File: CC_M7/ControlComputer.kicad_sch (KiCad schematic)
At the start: 38 parts, among them U1 STM32H743VITx, Y1 32MHz

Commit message: Scehmatic completed.
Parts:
- removed U1: STM32H743VITx, Package_QFP:LQFP-100_14x14mm_P0.5mm, symbol MCU_ST_STM32H7:STM32H743VITx
- added U1: STM32H743VGTx, Package_QFP:LQFP-100_14x14mm_P0.5mm, symbol MCU_ST_STM32H7:STM32H743VGTx
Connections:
- net +3.3V: now also U1.100 (VDD), U1.11 (VDD), U1.27 (VDD), U1.50 (VDD), U1.6 (VBAT), U1.75 (VDD)
- net BOOT0: now also U1.94 (BOOT0)
- net CAN2_RX: now also U1.51 (PB12)
- net CAN2_TX: now also U1.52 (PB13)
- net GND: now also U1.10 (VSS), U1.19 (VSSA), U1.26 (VSS), U1.49 (VSS), U1.74 (VSS), U1.99 (VSS)
- net HSE_IN: now also U1.12 (PH0)
- net HSE_OUT: now also U1.13 (PH1)
- net I2C1_IRQ1: now also U1.43 (PE13)
- net I2C1_IRQ2: now also U1.44 (PE14)
- net I2C1_SCL: now also U1.92 (PB6)
- net I2C1_SDA: now also U1.93 (PB7)
- net I2C2_SCL: now also U1.46 (PB10)
- net I2C2_SDA: now also U1.47 (PB11)
- net LED0: now also U1.40 (PE10)
- net LED1: now also U1.41 (PE11)
- net NRST: now also U1.14 (NRST)
- net PA0: now also U1.22 (PA0)
- net PA1: now also U1.23 (PA1)
- net PA4: now also U1.28 (PA4)
- net PC13: now also U1.7 (PC13)
- net PC14: now also U1.8 (PC14)
- net PC15: now also U1.9 (PC15)
- net PE2: now also U1.1 (PE2)
- net PE3: now also U1.2 (PE3)
- net PE4: now also U1.3 (PE4)
- net PE5: now also U1.4 (PE5)
- net PE6: now also U1.5 (PE6)
- net SPI1_CS1: now also U1.32 (PC4)
- net SPI1_CS2: now also U1.33 (PC5)
- net SPI1_CS3: now also U1.34 (PB0)
- net SPI1_MISO: now also U1.30 (PA6)
- net SPI1_MOSI: now also U1.31 (PA7)
- net SPI1_SCK: now also U1.29 (PA5)
- net SPI3_CS: now also U1.81 (PD0)
- net SPI3_IRQ: now also U1.82 (PD1)
- net SPI3_MISO: now also U1.79 (PC11)
- net SPI3_MOSI: now also U1.80 (PC12)
- net SPI3_SCK: now also U1.78 (PC10)
- net SWCLK: now also U1.76 (PA14)
- net SWDIO: now also U1.72 (PA13)
- net SWO: now also U1.89 (PB3)
- net TIM3_CH1: now also U1.63 (PC6)
- net TIM3_CH2: now also U1.64 (PC7)
- net TIM3_CH3: now also U1.65 (PC8)
- net TIM3_CH4: now also U1.66 (PC9)
- net TIM4_CH3: now also U1.61 (PD14)
- net TIM4_CH4: now also U1.62 (PD15)
- net UART1_RX: now also U1.69 (PA10)
- net UART1_TX: now also U1.68 (PA9)
- net UART2_RX: now also U1.25 (PA3)
- net UART2_TX: now also U1.24 (PA2)
- net UART3_RX: now also U1.56 (PD9)
- net UART3_TX: now also U1.55 (PD8)
- net UART4_RX: now also U1.95 (PB8)
- net UART4_TX: now also U1.96 (PB9)
- net USB_DM: now also U1.70 (PA11)
- net USB_DP: now also U1.71 (PA12)
- net VDDA_CC: now also U1.21 (VDDA)
- net VREF_CC: now also U1.20 (VREF+)
- net at C17.1: now also U1.48 (VCAP)
- net at C18.1: now also U1.73 (VCAP)
- no-connect marks 28 -> 29
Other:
- note removed: "STM32H743VGT6"
- moved on the sheet: C1, C10, C12, C13, C14, C15, C17, C18, C2, C20, C21, C4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

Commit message: last control
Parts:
- added JP9: SWDIO, jmpertest:jmpertest, symbol Jumper:Jumper_2_Bridged
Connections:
- net J2_38 is gone; now on net J2_36: JP3.2 (B)
- net +3.3V: now also JP9.1 (A)
- net J2_36: no longer JP2.2 (B)
- net SWDIO: now also JP1.1 (A); no longer JP3.1 (A)
- net SWO: now also JP3.1 (A); no longer JP1.1 (A)
- net PE5: no longer names the net of U1.4 (PE5)
- net PE6: no longer names the net of U1.5 (PE6)
- new net J2_31: JP9.2 (B)
- new net J2_34: JP2.2 (B)
- no-connect marks 29 -> 31
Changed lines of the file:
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@@
 	)
 	(no_connect
+		(at 45.72 147.32)
+	)
+	(no_connect
 		(at 45.72 190.5)
 	)
 	(no_connect
+		(at 45.72 149.86)
+	)
+	(no_connect
 		(at 45.72 210.82)
 	)
@@
 	(wire
 		(pts
+			(xy 152.4 200.66) (xy 160.02 200.66)
+		)
+		(stroke
+			(width 0)
+			(type default)
+		)
+	)
+	(wire
+		(pts
 			(xy 96.52 27.94) (xy 96.52 30.48)
 		)
@@
 		)
 	)
+	(global_label "J2_40"
+		(shape input)
+		(at 170.18 220.98 0)
+		(fields_autoplaced yes)
+		(effects
+			(font
+				(size 1.27 1.27)
+			)
+			(justify left)
+		)
+		(property "Intersheetrefs" "${INTERSHEET_REFS}"
+			(at 178.7289 220.98 0)
+			(effects
+				(font
+					(size 1.27 1.27)
+				)
+				(justify left)
+				(hide yes)
+			)
+		)
+	)
 	(global_label "UART1_TX"
 		(shape input)
@@
 		)
 	)
+	(global_label "J2_36"
+		(shape input)
+		(at 170.18 215.9 0)
+		(fields_autoplaced yes)
+		(effects
+			(font
+				(size 1.27 1.27)
+			)
+			(justify left)
+		)
+		(property "Intersheetrefs" "${INTERSHEET_REFS}"
+			(at 178.7289 215.9 0)
+			(effects
+				(font
+					(size 1.27 1.27)
+				)
+				(justify left)
+				(hide yes)
+			)
+		)
+	)
 	(global_label "LED0"
 		(shape input)
@@
 	(global_label "SWO"
 		(shape input)
-		(at 160.02 205.74 180)
+		(at 160.02 215.9 180)
 		(fields_autoplaced yes)
 		(effects
@@
 		)
 		(property "Intersheetrefs" "${INTERSHEET_REFS}"
-			(at 153.0434 205.74 0)
+			(at 153.0434 215.9 0)
 			(effects
 				(font
@@
 		)
 	)
+	(global_label "J2_32"
+		(shape input)
+		(at 170.18 205.74 0)
+		(fields_autoplaced yes)
+		(effects
+			(font
+				(size 1.27 1.27)
+			)
+			(justify left)
+		)
+		(property "Intersheetrefs" "${INTERSHEET_REFS}"
+			(at 178.7289 205.74 0)
+			(effects
+				(font
+					(size 1.27 1.27)
+				)
+				(justify left)
+				(hide yes)
+			)
+		)
+	)
 	(global_label "UART4_RX"
 		(shape input)
@@
 		)
 	)
+	(global_label "J2_31"
+		(shape input)
+		(at 170.18 200.66 0)
+		(fields_autoplaced yes)
+		(effects
+			(font
+				(size 1.27 1.27)
+			)
+			(justify left)
+		)
+		(property "Intersheetrefs" "${INTERSHEET_REFS}"
+			(at 178.7289 200.66 0)
+			(effects
+				(font
+					(size 1.27 1.27)
+				)
+				(justify left)
+				(hide yes)
+			)
+		)
+	)
 	(global_label "SPI1_CS1"
 		(shape input)
@@
 		)
 	)
+	(global_label "J2_34"
+		(shape input)
+		(at 170.18 210.82 0)
+		(fields_autoplaced yes)
+		(effects
+			(font
+				(size 1.27 1.27)
+			)
+			(justify left)
+		)
+		(property "Intersheetrefs" "${INTERSHEET_REFS}"
+			(at 178.7289 210.82 0)
+			(effects
+				(font
+					(size 1.27 1.27)
+				)
+				(justify left)
+				(hide yes)
+			)
+		)
+	)
 	(global_label "SWDIO"
 		(shape input)
-		(at 160.02 215.9 180)
+		(at 160.02 205.74 180)
 		(fields_autoplaced yes)
 		(effects
@@
 		)
 		(property "Intersheetrefs" "${INTERSHEET_REFS}"
-			(at 151.1686 215.9 0)
+			(at 151.1686 205.74 0)
 			(effects
 				(font
@@
 		)
 	)
-	(global_label "PE6"
-		(shape input)
-		(at 45.72 149.86 180)
-		(fields_autoplaced yes)
-		(effects
-			(font
-				(size 1.27 1.27)
-			)
-			(justify right)
-		)
-		(property "Intersheetrefs" "${INTERSHEET_REFS}"
-			(at 39.1063 149.86 0)
-			(effects
-				(font
-					(size 1.27 1.27)
-				)
-				(justify right)
-				(hide yes)
-			)
-		)
-	)
-	(global_label "J2_40"
-		(shape input)
-		(at 170.18 220.98 0)
-		(fields_autoplaced yes)
-		(effects
-			(font
-				(size 1.27 1.27)
-			)
-			(justify left)
-		)
-		(property "Intersheetrefs" "${INTERSHEET_REFS}"
-			(at 178.7289 220.98 0)
-			(effects
-				(font
-					(size 1.27 1.27)
-				)
-				(justify left)
-				(hide yes)
-			)
-		)
-	)
 	(global_label "SPI3_SCK"
 		(shape input)
@@
 		)
 	)
-	(global_label "PE5"
-		(shape input)
-		(at 45.72 147.32 180)
-		(fields_autoplaced yes)
-		(effects
-			(font
-				(size 1.27 1.27)
-			)
-			(justify right)
-		)
-		(property "Intersheetrefs" "${INTERSHEET_REFS}"
-			(at 39.1063 147.32 0)
-			(effects
-				(font
-					(size 1.27 1.27)
-				)
-				(justify right)
-				(hide yes)
-			)
-		)
-	)
 	(global_label "HSE_OUT"
 		(shape input)
@@
 		)
 	)
-	(global_label "J2_32"
-		(shape input)
-		(at 170.18 205.74 0)
-		(fields_autoplaced yes)
-		(effects
-			(font
-				(size 1.27 1.27)
-			)
-			(justify left)
-		)
-		(property "Intersheetrefs" "${INTERSHEET_REFS}"
-			(at 178.7289 205.74 0)
-			(effects
-				(font
-					(size 1.27 1.27)
-				)
-				(justify left)
-				(hide yes)
-			)
-		)
-	)
 	(global_label "NRST"
 		(shape input)
@@
 		)
 	)
-	(global_label "J2_38"
-		(shape input)
-		(at 170.18 215.9 0)
-		(fields_autoplaced yes)
-		(effects
-			(font
-				(size 1.27 1.27)
-			)
-			(justify left)
-		)
-		(property "Intersheetrefs" "${INTERSHEET_REFS}"
-			(at 178.7289 215.9 0)
-			(effects
-				(font
-					(size 1.27 1.27)
-				)
-				(justify left)
-				(hide yes)
-			)
-		)
-	)
-	(global_label "J2_36"
-		(shape input)
-		(at 170.18 210.82 0)
-		(fields_autoplaced yes)
-		(effects
-			(font
-				(size 1.27 1.27)
-			)
-			(justify left)
-		)
-		(property "Intersheetrefs" "${INTERSHEET_REFS}"
-			(at 178.7289 210.82 0)
-			(effects
-				(font
-					(size 1.27 1.27)
-				)
-				(justify left)
-				(hide yes)
-			)
-		)
-	)
 	(global_label "PA1"
 		(shape input)
@@
 	)
 	(symbol
+		(lib_id "Jumper:Jumper_2_Bridged")
+		(at 165.1 200.66 0)
+		(unit 1)
+		(exclude_from_sim yes)
+		(in_bom yes)
+		(on_board yes)
+		(dnp no)
+		(property "Reference" "JP9"
+			(at 165.1 198.12 0)
+			(effects
+				(font
+					(size 1.27 1.27)
+				)
+			)
+		)
+		(property "Value" "SWDIO"
+			(at 165.1 198.12 0)
+			(effects
+				(font
+					(size 1.27 1.27)
+				)
+				(hide yes)
+			)
+		)
+		(property "Footprint" "jmpertest:jmpertest"
+			(at 165.1 200.66 0)
+			(effects
+				(font
+					(size 1.27 1.27)
+				)
+				(hide yes)
+			)
+		)
+		(property "Datasheet" "~"
+			(at 165.1 200.66 0)
+			(effects
+				(font
+					(size 1.27 1.27)
+				)
+				(hide yes)
+			)
+		)
+		(property "Description" "Jumper, 2-pole, closed/bridged"
+			(at 165.1 200.66 0)
+			(effects
+				(font
+					(size 1.27 1.27)
+				)
+				(hide yes)
+			)
+		)
+		(pin "2"
+		)
+		(pin "1"
+		)
+		(instances
+			(project "CC_M7"
+				(path "/20c3bbae-00c6-470e-8b69-dc0f665257a3/07f6f905-59c0-438f-a556-b28e89ace803"
+					(reference "JP9")
+					(unit 1)
+				)
+			)
+		)
+	)
+	(symbol
 		(lib_id "Device:R_Small")
 		(at 165.1 175.26 270)
@@
 					(unit 1)
 				)
+			)
+		)
+	)
+	(symbol
+		(lib_id "power:+3.3V")
+		(at 152.4 200.66 90)
+		(unit 1)
+		(exclude_from_sim no)
+		(in_bom yes)
+		(on_board yes)
+		(dnp no)
+		(fields_autoplaced yes)
+		(property "Reference" "#PWR039"
+			(at 156.21 200.66 0)
+			(effects
+				(font
+					(size 1.27 1.27)
+				)
+				(hide yes)
+			)
+		)
+		(property "Value" "+3.3V"
+			(at 148.59 200.6599 90)
+			(effects
+				(font
+					(size 1.27 1.27)
+				)
+				(justify left)
+			)
+		)
+		(property "Footprint" ""
+			(at 152.4 200.66 0)
+			(effects
+				(font
+					(size 1.27 1.27)
+				)
+				(hide yes)
+			)
+		)
+		(property "Datasheet" ""
+			(at 152.4 200.66 0)
+			(effects
+				(font
+					(size 1.27 1.27)
+				)
+				(hide yes)
+			)
+		)
+		(property "Description" "Power symbol creates a global label with name \"+3.3V\""
+			(at 152.4 200.66 0)
+			(effects
+				(font
+					(size 1.27 1.27)
+				)
+				(hide yes)
+			)
+		)
+		(pin "1"
+		)
+		(instances
+			(project "CC_M7"
+				(path "/20c3bbae-00c6-470e-8b69-dc0f665257a3/07f6f905-59c0-438f-a556-b28e89ace803"
+					(reference "#PWR039")
+					(unit 1)
+				)

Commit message: ready for routing
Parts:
- removed JP9: SWDIO, jmpertest:jmpertest, symbol Jumper:Jumper_2_Bridged
- added JP5: SWDIO, Jumper:SolderJumper-2_P1.3mm_Open_TrianglePad1.0x1.5mm, symbol Jumper:Jumper_2_Bridged
- C1: footprint Capacitor_SMD:C_0603_1608Metric -> Capacitor_SMD:C_0402_1005Metric
- JP1, JP2, JP3, JP4: footprint jmpertest:jmpertest -> Jumper:SolderJumper-2_P1.3mm_Open_TrianglePad1.0x1.5mm
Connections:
- net +3.3V: now also JP1.1 (A)
- net J2_31: now also JP1.2 (B)
- net J2_32: now also JP2.2 (B); no longer JP1.2 (B)
- net J2_34: now also JP3.2 (B); no longer JP2.2 (B)
- net J2_36: now also JP4.2 (B); no longer JP3.2 (B)
- net J2_40: now also JP5.2 (B); no longer JP4.2 (B)
- net NRST: now also JP5.1 (A); no longer JP4.1 (A)
- net SWCLK: now also JP3.1 (A); no longer JP2.1 (A)
- net SWDIO: now also JP2.1 (A); no longer JP1.1 (A)
- net SWO: now also JP4.1 (A); no longer JP3.1 (A)
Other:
- moved on the sheet: JP1, JP2, JP3, JP4
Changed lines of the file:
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@@
 	(text "OSC STM32"
 		(exclude_from_sim no)
-		(at 182.88 121.92 0)
+		(at 180.975 121.92 0)
 		(effects
 			(font
@@
 	(text "I2C PULL_UP"
 		(exclude_from_sim no)
-		(at 180.34 157.48 0)
+		(at 179.07 157.48 0)
 		(effects
 			(font
@@
 	(text "VDDA FILTER"
 		(exclude_from_sim no)
-		(at 116.84 83.82 0)
+		(at 115.57 83.82 0)
 		(effects
 			(font
@@
 	)
 	(symbol
-		(lib_id "Jumper:Jumper_2_Bridged")
-		(at 165.1 200.66 0)
-		(unit 1)
-		(exclude_from_sim yes)
-		(in_bom yes)
-		(on_board yes)
-		(dnp no)
-		(property "Reference" "JP9"
-			(at 165.1 198.12 0)
-			(effects
-				(font
-					(size 1.27 1.27)
-				)
-			)
-		)
-		(property "Value" "SWDIO"
-			(at 165.1 198.12 0)
-			(effects
-				(font
-					(size 1.27 1.27)
-				)
-				(hide yes)
-			)
-		)
-		(property "Footprint" "jmpertest:jmpertest"
-			(at 165.1 200.66 0)
-			(effects
-				(font
-					(size 1.27 1.27)
-				)
-				(hide yes)
-			)
-		)
-		(property "Datasheet" "~"
-			(at 165.1 200.66 0)
-			(effects
-				(font
-					(size 1.27 1.27)
-				)
-				(hide yes)
-			)
-		)
-		(property "Description" "Jumper, 2-pole, closed/bridged"
-			(at 165.1 200.66 0)
-			(effects
-				(font
-					(size 1.27 1.27)
-				)
-				(hide yes)
-			)
-		)
-		(pin "2"
-		)
-		(pin "1"
-		)
-		(instances
-			(project "CC_M7"
-				(path "/20c3bbae-00c6-470e-8b69-dc0f665257a3/07f6f905-59c0-438f-a556-b28e89ace803"
-					(reference "JP9")
-					(unit 1)
-				)
-			)
-		)
-	)
-	(symbol
 		(lib_id "Device:R_Small")
 		(at 165.1 175.26 270)
@@
 	(symbol
 		(lib_id "Jumper:Jumper_2_Bridged")
-		(at 165.1 220.98 0)
+		(at 165.1 215.9 0)
 		(unit 1)
 		(exclude_from_sim yes)
@@
 		(dnp no)
 		(property "Reference" "JP4"
-			(at 165.1 218.44 0)
+			(at 165.1 213.36 0)
 			(effects
 				(font
@@
 		)
 		(property "Value" "SWDIO"
-			(at 165.1 218.44 0)
+			(at 165.1 213.36 0)
 			(effects
 				(font
@@
 			)
 		)
-		(property "Footprint" "jmpertest:jmpertest"
-			(at 165.1 220.98 0)
+		(property "Footprint" "Jumper:SolderJumper-2_P1.3mm_Open_TrianglePad1.0x1.5mm"
+			(at 165.1 215.9 0)
 			(effects
 				(font
@@
 		)
 		(property "Datasheet" "~"
-			(at 165.1 220.98 0)
+			(at 165.1 215.9 0)
 			(effects
 				(font
@@
 		)
 		(property "Description" "Jumper, 2-pole, closed/bridged"
-			(at 165.1 220.98 0)
+			(at 165.1 215.9 0)
 			(effects
 				(font
@@
 	)
 	(symbol
+		(lib_id "Jumper:Jumper_2_Bridged")
+		(at 165.1 220.98 0)
+		(unit 1)
+		(exclude_from_sim yes)
+		(in_bom yes)
+		(on_board yes)
+		(dnp no)
+		(property "Reference" "JP5"
+			(at 165.1 218.44 0)
+			(effects
+				(font
+					(size 1.27 1.27)
+				)
+			)
+		)
+		(property "Value" "SWDIO"
+			(at 165.1 218.44 0)
+			(effects
+				(font
+					(size 1.27 1.27)
+				)
+				(hide yes)
+			)
+		)
+		(property "Footprint" "Jumper:SolderJumper-2_P1.3mm_Open_TrianglePad1.0x1.5mm"
+			(at 165.1 220.98 0)
+			(effects
+				(font
+					(size 1.27 1.27)
+				)
+				(hide yes)
+			)
+		)
+		(property "Datasheet" "~"
+			(at 165.1 220.98 0)
+			(effects
+				(font
+					(size 1.27 1.27)
+				)
+				(hide yes)
+			)
+		)
+		(property "Description" "Jumper, 2-pole, closed/bridged"
+			(at 165.1 220.98 0)
+			(effects
+				(font
+					(size 1.27 1.27)
+				)
+				(hide yes)
+			)
+		)
+		(pin "2"
+		)
+		(pin "1"
+		)
+		(instances
+			(project "CC_M7"
+				(path "/20c3bbae-00c6-470e-8b69-dc0f665257a3/07f6f905-59c0-438f-a556-b28e89ace803"
+					(reference "JP5")
+					(unit 1)
+				)
+			)
+		)
+	)
+	(symbol
 		(lib_id "Device:R_Small")
 		(at 162.56 142.24 180)
@@
 	(symbol
 		(lib_id "Jumper:Jumper_2_Bridged")
-		(at 165.1 210.82 0)
+		(at 165.1 205.74 0)
 		(unit 1)
 		(exclude_from_sim yes)
@@
 		(dnp no)
 		(property "Reference" "JP2"
-			(at 165.1 208.28 0)
+			(at 165.1 203.2 0)
 			(effects
 				(font
@@
 		)
 		(property "Value" "SWDIO"
-			(at 165.1 208.28 0)
+			(at 165.1 203.2 0)
 			(effects
 				(font
@@
 			)
 		)
-		(property "Footprint" "jmpertest:jmpertest"
-			(at 165.1 210.82 0)
+		(property "Footprint" "Jumper:SolderJumper-2_P1.3mm_Open_TrianglePad1.0x1.5mm"
+			(at 165.1 205.74 0)
 			(effects
 				(font
@@
 		)
 		(property "Datasheet" "~"
-			(at 165.1 210.82 0)
+			(at 165.1 205.74 0)
 			(effects
 				(font
@@
 		)
 		(property "Description" "Jumper, 2-pole, closed/bridged"
-			(at 165.1 210.82 0)
+			(at 165.1 205.74 0)
 			(effects
 				(font
@@
 	(symbol
 		(lib_id "Jumper:Jumper_2_Bridged")
-		(at 165.1 215.9 0)
+		(at 165.1 210.82 0)
 		(unit 1)
 		(exclude_from_sim yes)
@@
 		(dnp no)
 		(property "Reference" "JP3"
-			(at 165.1 213.36 0)
+			(at 165.1 208.28 0)
 			(effects
 				(font
@@
 		)
 		(property "Value" "SWDIO"
-			(at 165.1 213.36 0)
+			(at 165.1 208.28 0)
 			(effects
 				(font
@@
 			)
 		)
-		(property "Footprint" "jmpertest:jmpertest"
-			(at 165.1 215.9 0)
+		(property "Footprint" "Jumper:SolderJumper-2_P1.3mm_Open_TrianglePad1.0x1.5mm"
+			(at 165.1 210.82 0)
 			(effects
 				(font
@@
 		)
 		(property "Datasheet" "~"
-			(at 165.1 215.9 0)
+			(at 165.1 210.82 0)
 			(effects
 				(font
@@
 		)
 		(property "Description" "Jumper, 2-pole, closed/bridged"
-			(at 165.1 215.9 0)
+			(at 165.1 210.82 0)
 			(effects
 				(font
@@
 	(symbol
 		(lib_id "Jumper:Jumper_2_Bridged")
-		(at 165.1 205.74 0)
+		(at 165.1 200.66 0)
 		(unit 1)
 		(exclude_from_sim yes)
@@
 		(dnp no)
 		(property "Reference" "JP1"
-			(at 165.1 203.2 0)
+			(at 165.1 198.12 0)
 			(effects
 				(font
@@
 		)
 		(property "Value" "SWDIO"
-			(at 165.1 203.2 0)
+			(at 165.1 198.12 0)
 			(effects
 				(font
@@
 			)
 		)
-		(property "Footprint" "jmpertest:jmpertest"
-			(at 165.1 205.74 0)
+		(property "Footprint" "Jumper:SolderJumper-2_P1.3mm_Open_TrianglePad1.0x1.5mm"
+			(at 165.1 200.66 0)
 			(effects
 				(font
@@
 		)
 		(property "Datasheet" "~"
-			(at 165.1 205.74 0)
+			(at 165.1 200.66 0)
 			(effects
 				(font
@@
 		)
 		(property "Description" "Jumper, 2-pole, closed/bridged"
-			(at 165.1 205.74 0)
+			(at 165.1 200.66 0)
 			(effects
 				(font
@@
 			)
 		)
-		(property "Footprint" "Capacitor_SMD:C_0603_1608Metric"
+		(property "Footprint" "Capacitor_SMD:C_0402_1005Metric"
 			(at 40.64 33.02 0)
 			(effects

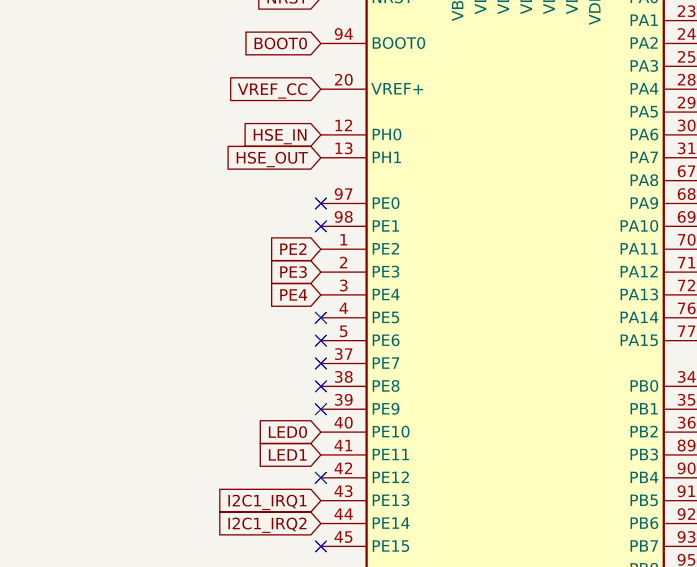
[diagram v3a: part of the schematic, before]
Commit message: ready to routing
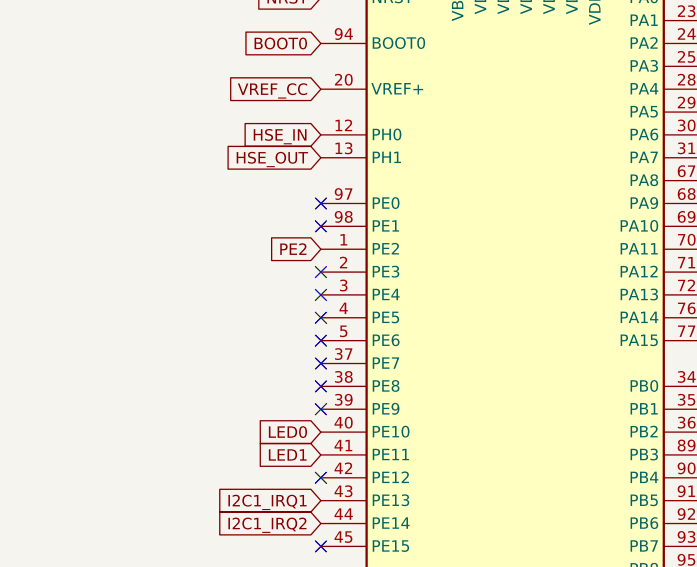
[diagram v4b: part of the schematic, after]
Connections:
- net PE3: no longer names the net of U1.2 (PE3)
- net PE4: no longer names the net of U1.3 (PE4)
- no-connect marks 31 -> 33

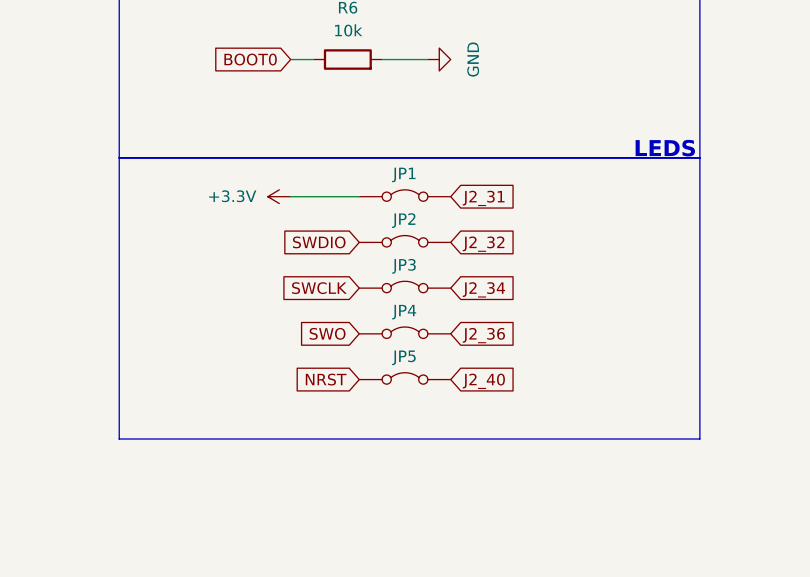
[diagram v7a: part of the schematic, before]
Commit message: Debugging routes added. / Debug footprint updated.
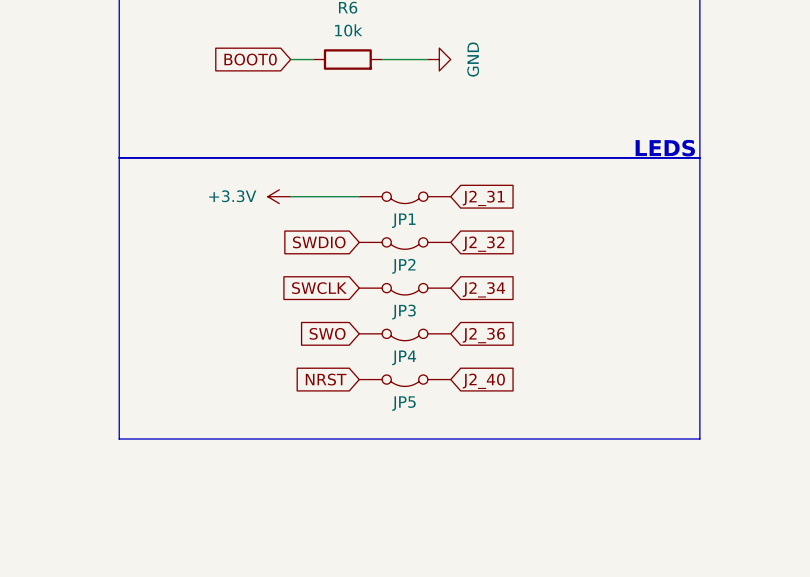
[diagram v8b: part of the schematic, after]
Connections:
- net +3.3V: now also JP1.2 (B); no longer JP1.1 (A)
- net J2_31: now also JP1.1 (A); no longer JP1.2 (B)
- net J2_32: now also JP2.1 (A); no longer JP2.2 (B)
- net J2_34: now also JP3.1 (A); no longer JP3.2 (B)
- net J2_36: now also JP4.1 (A); no longer JP4.2 (B)
- net J2_40: now also JP5.1 (A); no longer JP5.2 (B)
- net NRST: now also JP5.2 (B); no longer JP5.1 (A)
- net SWCLK: now also JP3.2 (B); no longer JP3.1 (A)
- net SWDIO: now also JP2.2 (B); no longer JP2.1 (A)
- net SWO: now also JP4.2 (B); no longer JP4.1 (A)
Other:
- moved on the sheet: JP1, JP2, JP3, JP4, JP5
